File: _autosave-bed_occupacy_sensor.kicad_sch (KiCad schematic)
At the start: 5 parts, among them J1 FSR_2, J2 FSR_1, U1 mini_esp32

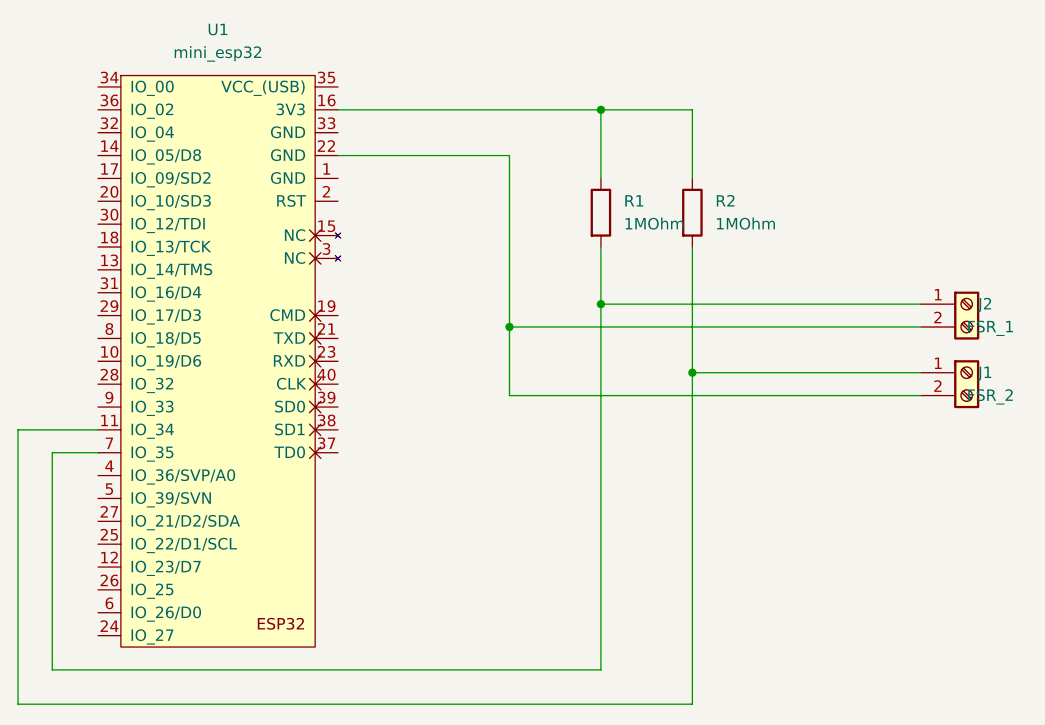
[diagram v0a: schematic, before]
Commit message: new pcb design all GND connected to ground plane
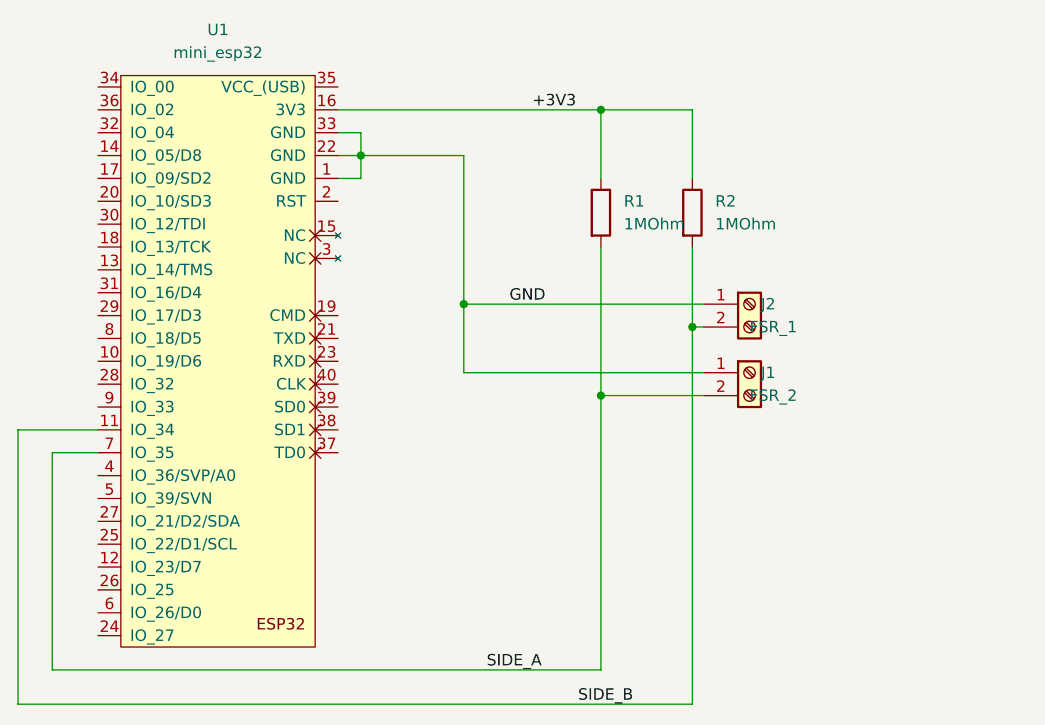
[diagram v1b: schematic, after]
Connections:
- net GND: now reaches U1.1 (GND)
- net GND: now also J1.1 (Pin_1), J2.1 (Pin_1), U1.22 (GND), U1.33 (GND)
- net SIDE_B: now reaches R2.2, U1.11 (IO_34)
- net SIDE_B: now also J2.2 (Pin_2); no longer J1.1 (Pin_1)
- net +3V3: now reaches R1.1, R2.1, U1.16 (3V3)
- net SIDE_A: now reaches R1.2, U1.7 (IO_35)
- net SIDE_A: now also J1.2 (Pin_2); no longer J2.1 (Pin_1)
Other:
- moved on the sheet: J1, J2
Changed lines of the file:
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@@
   (junction (at 113.03 26.67) (diameter 0) (color 0 0 0 0)
   )
-  (junction (at 102.87 50.8) (diameter 0) (color 0 0 0 0)
-  )
-  (junction (at 113.03 48.26) (diameter 0) (color 0 0 0 0)
-  )
-  (junction (at 123.19 55.88) (diameter 0) (color 0 0 0 0)
-  )
-  (wire (pts (xy 148.59 58.42) (xy 102.87 58.42))
-    (stroke (width 0) (type default) (color 0 0 0 0))
+  (junction (at 97.79 48.26) (diameter 0) (color 0 0 0 0)
+  )
+  (junction (at 123.19 50.8) (diameter 0) (color 0 0 0 0)
+  )
+  (junction (at 86.36 31.75) (diameter 0) (color 0 0 0 0)
+  )
+  (junction (at 113.03 58.42) (diameter 0) (color 0 0 0 0)
   )
   (wire (pts (xy 123.19 92.71) (xy 48.26 92.71))
     (stroke (width 0) (type default) (color 0 0 0 0))
   )
-  (wire (pts (xy 148.59 48.26) (xy 113.03 48.26))
-    (stroke (width 0) (type default) (color 0 0 0 0))
-  )
-  (wire (pts (xy 83.82 31.75) (xy 102.87 31.75))
-    (stroke (width 0) (type default) (color 0 0 0 0))
-  )
-  (wire (pts (xy 113.03 41.91) (xy 113.03 48.26))
+  (wire (pts (xy 83.82 34.29) (xy 86.36 34.29))
+    (stroke (width 0) (type default) (color 0 0 0 0))
+  )
+  (wire (pts (xy 124.46 55.88) (xy 97.79 55.88))
+    (stroke (width 0) (type default) (color 0 0 0 0))
+  )
+  (wire (pts (xy 86.36 31.75) (xy 83.82 31.75))
+    (stroke (width 0) (type default) (color 0 0 0 0))
+  )
+  (wire (pts (xy 113.03 41.91) (xy 113.03 58.42))
     (stroke (width 0) (type default) (color 0 0 0 0))
   )
@@
     (stroke (width 0) (type default) (color 0 0 0 0))
   )
+  (wire (pts (xy 123.19 50.8) (xy 124.46 50.8))
+    (stroke (width 0) (type default) (color 0 0 0 0))
+  )
   (wire (pts (xy 52.07 88.9) (xy 52.07 64.77))
     (stroke (width 0) (type default) (color 0 0 0 0))
   )
-  (wire (pts (xy 123.19 55.88) (xy 148.59 55.88))
-    (stroke (width 0) (type default) (color 0 0 0 0))
-  )
   (wire (pts (xy 113.03 26.67) (xy 113.03 34.29))
     (stroke (width 0) (type default) (color 0 0 0 0))
@@
     (stroke (width 0) (type default) (color 0 0 0 0))
   )
-  (wire (pts (xy 113.03 48.26) (xy 113.03 88.9))
+  (wire (pts (xy 113.03 58.42) (xy 113.03 88.9))
     (stroke (width 0) (type default) (color 0 0 0 0))
   )
@@
     (stroke (width 0) (type default) (color 0 0 0 0))
   )
+  (wire (pts (xy 83.82 29.21) (xy 86.36 29.21))
+    (stroke (width 0) (type default) (color 0 0 0 0))
+  )
   (wire (pts (xy 123.19 26.67) (xy 123.19 34.29))
     (stroke (width 0) (type default) (color 0 0 0 0))
   )
-  (wire (pts (xy 123.19 41.91) (xy 123.19 55.88))
+  (wire (pts (xy 86.36 29.21) (xy 86.36 31.75))
+    (stroke (width 0) (type default) (color 0 0 0 0))
+  )
+  (wire (pts (xy 123.19 41.91) (xy 123.19 50.8))
+    (stroke (width 0) (type default) (color 0 0 0 0))
+  )
+  (wire (pts (xy 97.79 31.75) (xy 86.36 31.75))
+    (stroke (width 0) (type default) (color 0 0 0 0))
+  )
+  (wire (pts (xy 113.03 58.42) (xy 124.46 58.42))
+    (stroke (width 0) (type default) (color 0 0 0 0))
+  )
+  (wire (pts (xy 123.19 50.8) (xy 123.19 92.71))
     (stroke (width 0) (type default) (color 0 0 0 0))
   )
@@
     (stroke (width 0) (type default) (color 0 0 0 0))
   )
-  (wire (pts (xy 102.87 50.8) (xy 102.87 58.42))
-    (stroke (width 0) (type default) (color 0 0 0 0))
-  )
-  (wire (pts (xy 102.87 50.8) (xy 148.59 50.8))
-    (stroke (width 0) (type default) (color 0 0 0 0))
-  )
-  (wire (pts (xy 123.19 55.88) (xy 123.19 92.71))
-    (stroke (width 0) (type default) (color 0 0 0 0))
-  )
-  (wire (pts (xy 102.87 31.75) (xy 102.87 50.8))
-    (stroke (width 0) (type default) (color 0 0 0 0))
+  (wire (pts (xy 86.36 34.29) (xy 86.36 31.75))
+    (stroke (width 0) (type default) (color 0 0 0 0))
+  )
+  (wire (pts (xy 124.46 48.26) (xy 97.79 48.26))
+    (stroke (width 0) (type default) (color 0 0 0 0))
+  )
+  (wire (pts (xy 97.79 48.26) (xy 97.79 31.75))
+    (stroke (width 0) (type default) (color 0 0 0 0))
+  )
+  (wire (pts (xy 97.79 55.88) (xy 97.79 48.26))
+    (stroke (width 0) (type default) (color 0 0 0 0))
+  )
+  (label "SIDE_A" (at 100.33 88.9 0)
+    (effects (font (size 1.27 1.27)) (justify left bottom))
+  )
+  (label "GND" (at 102.87 48.26 0)
+    (effects (font (size 1.27 1.27)) (justify left bottom))
+  )
+  (label "SIDE_B" (at 110.49 92.71 0)
+    (effects (font (size 1.27 1.27)) (justify left bottom))
+  )
+  (label "+3V3" (at 105.41 26.67 0)
+    (effects (font (size 1.27 1.27)) (justify left bottom))
   )
   (symbol (lib_id "ESP32_Mini:mini_esp32") (at 69.85 21.59 0) (unit 1)
@@
     (pin "2")
   )
-  (symbol (lib_id "Connector:Screw_Terminal_01x02") (at 153.67 48.26 0) (unit 1)
+  (symbol (lib_id "Connector:Screw_Terminal_01x02") (at 129.54 48.26 0) (unit 1)
     (in_bom yes) (on_board yes)
-    (property "Reference" "J2" (id 0) (at 154.94 48.2599 0)
-      (effects (font (size 1.27 1.27)) (justify left))
-    )
-    (property "Value" "FSR_1" (id 1) (at 153.67 50.8 0)
-      (effects (font (size 1.27 1.27)) (justify left))
-    )
-    (property "Footprint" "TerminalBlock:TerminalBlock_Altech_AK300-2_P5.00mm" (id 2) (at 153.67 48.26 0)
-      (effects (font (size 1.27 1.27)) hide)
-    )
-    (property "Datasheet" "~" (id 3) (at 153.67 48.26 0)
+    (property "Reference" "J2" (id 0) (at 130.81 48.2599 0)
+      (effects (font (size 1.27 1.27)) (justify left))
+    )
+    (property "Value" "FSR_1" (id 1) (at 129.54 50.8 0)
+      (effects (font (size 1.27 1.27)) (justify left))
+    )
+    (property "Footprint" "TerminalBlock:TerminalBlock_Altech_AK300-2_P5.00mm" (id 2) (at 129.54 48.26 0)
+      (effects (font (size 1.27 1.27)) hide)
+    )
+    (property "Datasheet" "~" (id 3) (at 129.54 48.26 0)
       (effects (font (size 1.27 1.27)) hide)
     )
@@
     (pin "2")
   )
-  (symbol (lib_id "Connector:Screw_Terminal_01x02") (at 153.67 55.88 0) (unit 1)
+  (symbol (lib_id "Connector:Screw_Terminal_01x02") (at 129.54 55.88 0) (unit 1)
     (in_bom yes) (on_board yes)
-    (property "Reference" "J1" (id 0) (at 154.94 55.8799 0)
-      (effects (font (size 1.27 1.27)) (justify left))
-    )
-    (property "Value" "FSR_2" (id 1) (at 153.67 58.42 0)
-      (effects (font (size 1.27 1.27)) (justify left))
-    )
-    (property "Footprint" "TerminalBlock:TerminalBlock_Altech_AK300-2_P5.00mm" (id 2) (at 153.67 55.88 0)
-      (effects (font (size 1.27 1.27)) hide)
-    )
-    (property "Datasheet" "~" (id 3) (at 153.67 55.88 0)
-      (effects (font (size 1.27 1.27)) hide)
-    )
+    (property "Reference" "J1" (id 0) (at 130.81 55.8799 0)
+      (effects (font (size 1.27 1.27)) (justify left))
+    )
+    (property "Value" "FSR_2" (id 1) (at 129.54 58.42 0)
+      (effects (font (size 1.27 1.27)) (justify left))
+    )
+    (property "Footprint" "TerminalBlock:TerminalBlock_Altech_AK300-2_P5.00mm" (id 2) (at 129.54 55.88 0)
+      (effects (font (size 1.27 1.27)) hide)
+    )
+    (property "Datasheet" "~" (id 3) (at 129.54 55.88 0)
+      (effects (font (size 1.27 1.27)) hide)
+    )
